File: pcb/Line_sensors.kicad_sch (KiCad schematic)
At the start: 28 parts, among them U10 CNY70, U4 CNY70, U5 CNY70, U6 CNY70, U7 CNY70, U8 CNY70, U9 CNY70

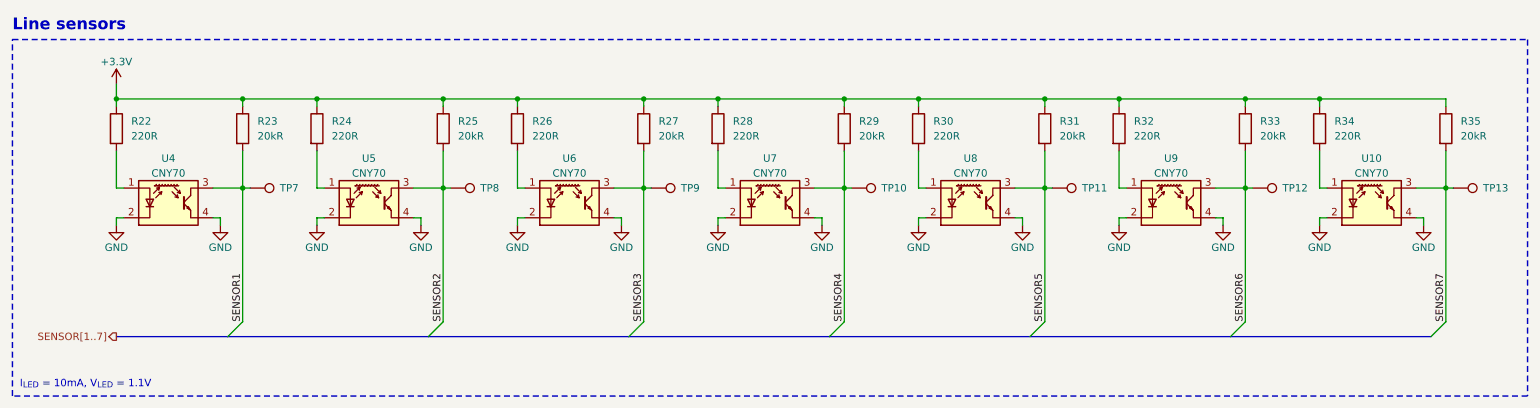
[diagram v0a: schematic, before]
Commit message: [pcb] Line sensors changed to pull-down and re-routed
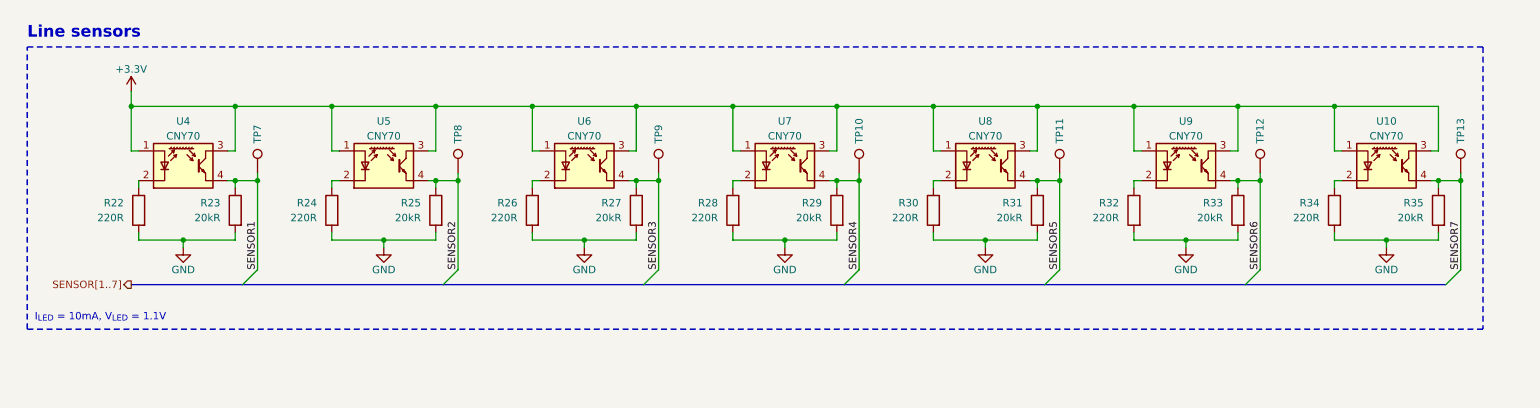
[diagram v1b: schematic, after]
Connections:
- net +3.3V: now also U10.1 (A), U10.3 (C), U4.1 (A), U4.3 (C), U5.1 (A), U5.3 (C), U6.1 (A), U6.3 (C), U7.1 (A), U7.3 (C), U8.1 (A), U8.3 (C), U9.1 (A), U9.3 (C); no longer R22.1, R23.1, R24.1, R25.1, R26.1, R27.1, R28.1, R29.1, R30.1, R31.1, R32.1, R33.1, R34.1, R35.1
- net GND: now also R22.2, R23.2, R24.2, R25.2, R26.2, R27.2, R28.2, R29.2, R30.2, R31.2, R32.2, R33.2, R34.2, R35.2; no longer U10.2 (K), U10.4 (E), U4.2 (K), U4.4 (E), U5.2 (K), U5.4 (E), U6.2 (K), U6.4 (E), U7.2 (K), U7.4 (E), U8.2 (K), U8.4 (E), U9.2 (K), U9.4 (E)
- net SENSOR1: now also R23.1, U4.4 (E); no longer R23.2, U4.3 (C)
- net SENSOR2: now also R25.1, U5.4 (E); no longer R25.2, U5.3 (C)
- net SENSOR3: now also R27.1, U6.4 (E); no longer R27.2, U6.3 (C)
- net SENSOR4: now also R29.1, U7.4 (E); no longer R29.2, U7.3 (C)
- net SENSOR5: now also R31.1, U8.4 (E); no longer R31.2, U8.3 (C)
- net SENSOR6: now also R33.1, U9.4 (E); no longer R33.2, U9.3 (C)
- net SENSOR7: now also R35.1, U10.4 (E); no longer R35.2, U10.3 (C)
- new net: R24.1, U5.2 (K)
- new net: R34.1, U10.2 (K)
- new net: R22.1, U4.2 (K)
- new net: R28.1, U7.2 (K)
- new net: R30.1, U8.2 (K)
- new net: R26.1, U6.2 (K)
- new net: R32.1, U9.2 (K)
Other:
- moved on the sheet: R22, TP7, U4

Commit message: [pcb] Test points reduced to 1.5mm; flow control series resistors added
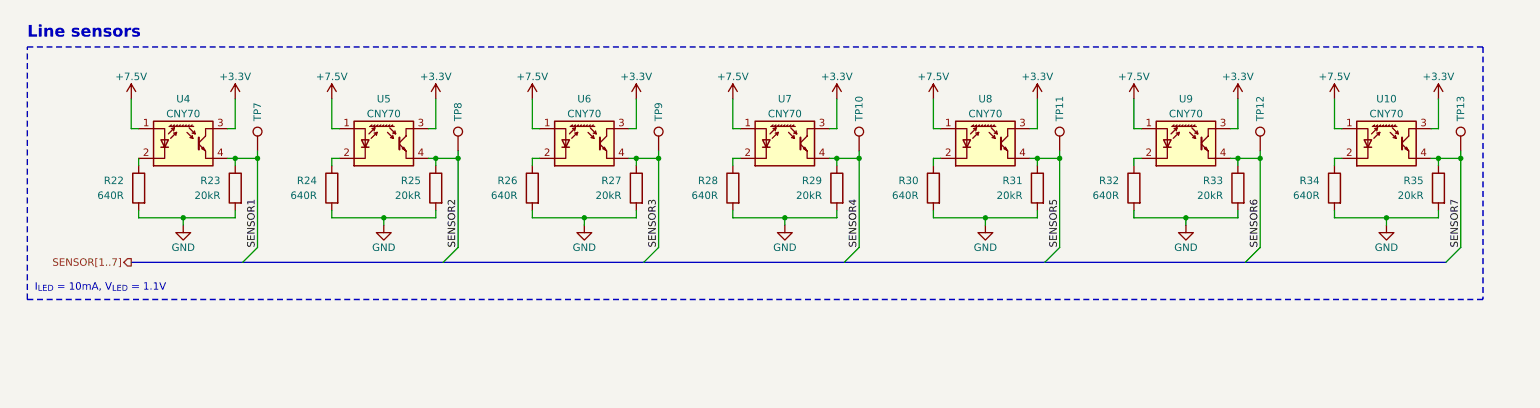
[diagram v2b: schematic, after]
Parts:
- R22, R24, R26, R28, R30, R32, R34: value 220R -> 640R
- TP10, TP11, TP12, TP13, TP7, TP8, TP9: footprint TestPoint:TestPoint_Pad_D2.0mm -> TestPoint:TestPoint_Pad_D1.5mm
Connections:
- net +3.3V: no longer U10.1 (A), U4.1 (A), U5.1 (A), U6.1 (A), U7.1 (A), U8.1 (A), U9.1 (A)
- new net +7.5V: U10.1 (A), U4.1 (A), U5.1 (A), U6.1 (A), U7.1 (A), U8.1 (A), U9.1 (A)
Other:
- moved on the sheet: R22, R23, R24, R25, R26, R27, R28, R29, R30, R31, R32, R33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

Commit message: [pcb] Rename line sensors to S1..S7
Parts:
- renumbered U4 to S1, U5 to S2, U6 to S3, U7 to S4, U8 to S5, U9 to S6, U10 to S7
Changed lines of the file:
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@@
   (symbol (lib_id "Sensor_Proximity:CNY70") (at 78.74 36.83 0) (unit 1)
     (in_bom yes) (on_board yes) (dnp no) (fields_autoplaced)
-    (property "Reference" "U5" (at 78.74 29.21 0)
+    (property "Reference" "S2" (at 78.74 29.21 0)
       (effects (font (size 1.27 1.27)))
     )
@@
       (project "Autko"
         (path "/8d5cfdec-de34-4148-9100-7125640c46f5/80d635c6-4a73-4538-989a-c930c6a7f33b"
-          (reference "U5") (unit 1)
+          (reference "S2") (unit 1)
         )
       )
@@
   (symbol (lib_id "Sensor_Proximity:CNY70") (at 250.19 36.83 0) (unit 1)
     (in_bom yes) (on_board yes) (dnp no) (fields_autoplaced)
-    (property "Reference" "U10" (at 250.19 29.21 0)
+    (property "Reference" "S7" (at 250.19 29.21 0)
       (effects (font (size 1.27 1.27)))
     )
@@
       (project "Autko"
         (path "/8d5cfdec-de34-4148-9100-7125640c46f5/80d635c6-4a73-4538-989a-c930c6a7f33b"
-          (reference "U10") (unit 1)
+          (reference "S7") (unit 1)
         )
       )
@@
   (symbol (lib_id "Sensor_Proximity:CNY70") (at 147.32 36.83 0) (unit 1)
     (in_bom yes) (on_board yes) (dnp no) (fields_autoplaced)
-    (property "Reference" "U7" (at 147.32 29.21 0)
+    (property "Reference" "S4" (at 147.32 29.21 0)
       (effects (font (size 1.27 1.27)))
     )
@@
       (project "Autko"
         (path "/8d5cfdec-de34-4148-9100-7125640c46f5/80d635c6-4a73-4538-989a-c930c6a7f33b"
-          (reference "U7") (unit 1)
+          (reference "S4") (unit 1)
         )
       )
@@
   (symbol (lib_id "Sensor_Proximity:CNY70") (at 181.61 36.83 0) (unit 1)
     (in_bom yes) (on_board yes) (dnp no) (fields_autoplaced)
-    (property "Reference" "U8" (at 181.61 29.21 0)
+    (property "Reference" "S5" (at 181.61 29.21 0)
       (effects (font (size 1.27 1.27)))
     )
@@
       (project "Autko"
         (path "/8d5cfdec-de34-4148-9100-7125640c46f5/80d635c6-4a73-4538-989a-c930c6a7f33b"
-          (reference "U8") (unit 1)
+          (reference "S5") (unit 1)
         )
       )
@@
   (symbol (lib_id "Sensor_Proximity:CNY70") (at 113.03 36.83 0) (unit 1)
     (in_bom yes) (on_board yes) (dnp no) (fields_autoplaced)
-    (property "Reference" "U6" (at 113.03 29.21 0)
+    (property "Reference" "S3" (at 113.03 29.21 0)
       (effects (font (size 1.27 1.27)))
     )
@@
       (project "Autko"
         (path "/8d5cfdec-de34-4148-9100-7125640c46f5/80d635c6-4a73-4538-989a-c930c6a7f33b"
-          (reference "U6") (unit 1)
+          (reference "S3") (unit 1)
         )
       )
@@
   (symbol (lib_id "Sensor_Proximity:CNY70") (at 215.9 36.83 0) (unit 1)
     (in_bom yes) (on_board yes) (dnp no) (fields_autoplaced)
-    (property "Reference" "U9" (at 215.9 29.21 0)
+    (property "Reference" "S6" (at 215.9 29.21 0)
       (effects (font (size 1.27 1.27)))
     )
@@
       (project "Autko"
         (path "/8d5cfdec-de34-4148-9100-7125640c46f5/80d635c6-4a73-4538-989a-c930c6a7f33b"
-          (reference "U9") (unit 1)
+          (reference "S6") (unit 1)
         )
       )
@@
   (symbol (lib_id "Sensor_Proximity:CNY70") (at 44.45 36.83 0) (unit 1)
     (in_bom yes) (on_board yes) (dnp no) (fields_autoplaced)
-    (property "Reference" "U4" (at 44.45 29.21 0)
+    (property "Reference" "S1" (at 44.45 29.21 0)
       (effects (font (size 1.27 1.27)))
     )
@@
       (project "Autko"
         (path "/8d5cfdec-de34-4148-9100-7125640c46f5/80d635c6-4a73-4538-989a-c930c6a7f33b"
-          (reference "U4") (unit 1)
-        )
-      )
+          (reference "S1") (unit 1)
+        )
+      )

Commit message: [pcb] Assign smaller footprints
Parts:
- R22, R23, R24, R25, R26, R27, R28, R29, R30, R31, R32, R33, R34, R35: footprint Resistor_SMD:R_0805_2012Metric -> Resistor_SMD:R_0603_1608Metric
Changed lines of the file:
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@@
       (effects (font (size 1.27 1.27)) (justify left))
     )
-    (property "Footprint" "Resistor_SMD:R_0805_2012Metric" (at 260.858 44.45 90)
+    (property "Footprint" "Resistor_SMD:R_0603_1608Metric" (at 260.858 44.45 90)
       (effects (font (size 1.27 1.27)) hide)
     )
@@
       (effects (font (size 1.27 1.27)) (justify left))
     )
-    (property "Footprint" "Resistor_SMD:R_0805_2012Metric" (at 89.408 44.45 90)
+    (property "Footprint" "Resistor_SMD:R_0603_1608Metric" (at 89.408 44.45 90)
       (effects (font (size 1.27 1.27)) hide)
     )
@@
       (effects (font (size 1.27 1.27)) (justify left))
     )
-    (property "Footprint" "Resistor_SMD:R_0805_2012Metric" (at 55.118 44.45 90)
+    (property "Footprint" "Resistor_SMD:R_0603_1608Metric" (at 55.118 44.45 90)
       (effects (font (size 1.27 1.27)) hide)
     )
@@
       (effects (font (size 1.27 1.27)) (justify left))
     )
-    (property "Footprint" "Resistor_SMD:R_0805_2012Metric" (at 38.608 44.45 90)
+    (property "Footprint" "Resistor_SMD:R_0603_1608Metric" (at 38.608 44.45 90)
       (effects (font (size 1.27 1.27)) hide)
     )
@@
       (effects (font (size 1.27 1.27)) (justify left))
     )
-    (property "Footprint" "Resistor_SMD:R_0805_2012Metric" (at 226.568 44.45 90)
+    (property "Footprint" "Resistor_SMD:R_0603_1608Metric" (at 226.568 44.45 90)
       (effects (font (size 1.27 1.27)) hide)
     )
@@
       (effects (font (size 1.27 1.27)) (justify left))
     )
-    (property "Footprint" "Resistor_SMD:R_0805_2012Metric" (at 71.628 44.45 90)
+    (property "Footprint" "Resistor_SMD:R_0603_1608Metric" (at 71.628 44.45 90)
       (effects (font (size 1.27 1.27)) hide)
     )
@@
       (effects (font (size 1.27 1.27)) (justify left))
     )
-    (property "Footprint" "Resistor_SMD:R_0805_2012Metric" (at 192.278 44.45 90)
+    (property "Footprint" "Resistor_SMD:R_0603_1608Metric" (at 192.278 44.45 90)
       (effects (font (size 1.27 1.27)) hide)
     )
@@
       (effects (font (size 1.27 1.27)) (justify left))
     )
-    (property "Footprint" "Resistor_SMD:R_0805_2012Metric" (at 105.918 44.45 90)
+    (property "Footprint" "Resistor_SMD:R_0603_1608Metric" (at 105.918 44.45 90)
       (effects (font (size 1.27 1.27)) hide)
     )
@@
       (effects (font (size 1.27 1.27)) (justify left))
     )
-    (property "Footprint" "Resistor_SMD:R_0805_2012Metric" (at 140.208 44.45 90)
+    (property "Footprint" "Resistor_SMD:R_0603_1608Metric" (at 140.208 44.45 90)
       (effects (font (size 1.27 1.27)) hide)
     )
@@
       (effects (font (size 1.27 1.27)) (justify left))
     )
-    (property "Footprint" "Resistor_SMD:R_0805_2012Metric" (at 123.698 44.45 90)
+    (property "Footprint" "Resistor_SMD:R_0603_1608Metric" (at 123.698 44.45 90)
       (effects (font (size 1.27 1.27)) hide)
     )
@@
       (effects (font (size 1.27 1.27)) (justify left))
     )
-    (property "Footprint" "Resistor_SMD:R_0805_2012Metric" (at 174.498 44.45 90)
+    (property "Footprint" "Resistor_SMD:R_0603_1608Metric" (at 174.498 44.45 90)
       (effects (font (size 1.27 1.27)) hide)
     )
@@
       (effects (font (size 1.27 1.27)) (justify left))
     )
-    (property "Footprint" "Resistor_SMD:R_0805_2012Metric" (at 208.788 44.45 90)
+    (property "Footprint" "Resistor_SMD:R_0603_1608Metric" (at 208.788 44.45 90)
       (effects (font (size 1.27 1.27)) hide)
     )
@@
       (effects (font (size 1.27 1.27)) (justify left))
     )
-    (property "Footprint" "Resistor_SMD:R_0805_2012Metric" (at 157.988 44.45 90)
+    (property "Footprint" "Resistor_SMD:R_0603_1608Metric" (at 157.988 44.45 90)
       (effects (font (size 1.27 1.27)) hide)
     )
@@
       (effects (font (size 1.27 1.27)) (justify left))
     )
-    (property "Footprint" "Resistor_SMD:R_0805_2012Metric" (at 243.078 44.45 90)
-      (effects (font (size 1.27 1.27)) hide)
-    )
+    (property "Footprint" "Resistor_SMD:R_0603_1608Metric" (at 243.078 44.45 90)
+      (effects (font (size 1.27 1.27)) hide)
+    )
